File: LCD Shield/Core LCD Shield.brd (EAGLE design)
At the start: 38.1 x 35.6 mm, 9 parts, among them IC1 MC33269T-5.0, J1 TWIG_2.0-DIP-FEMALE

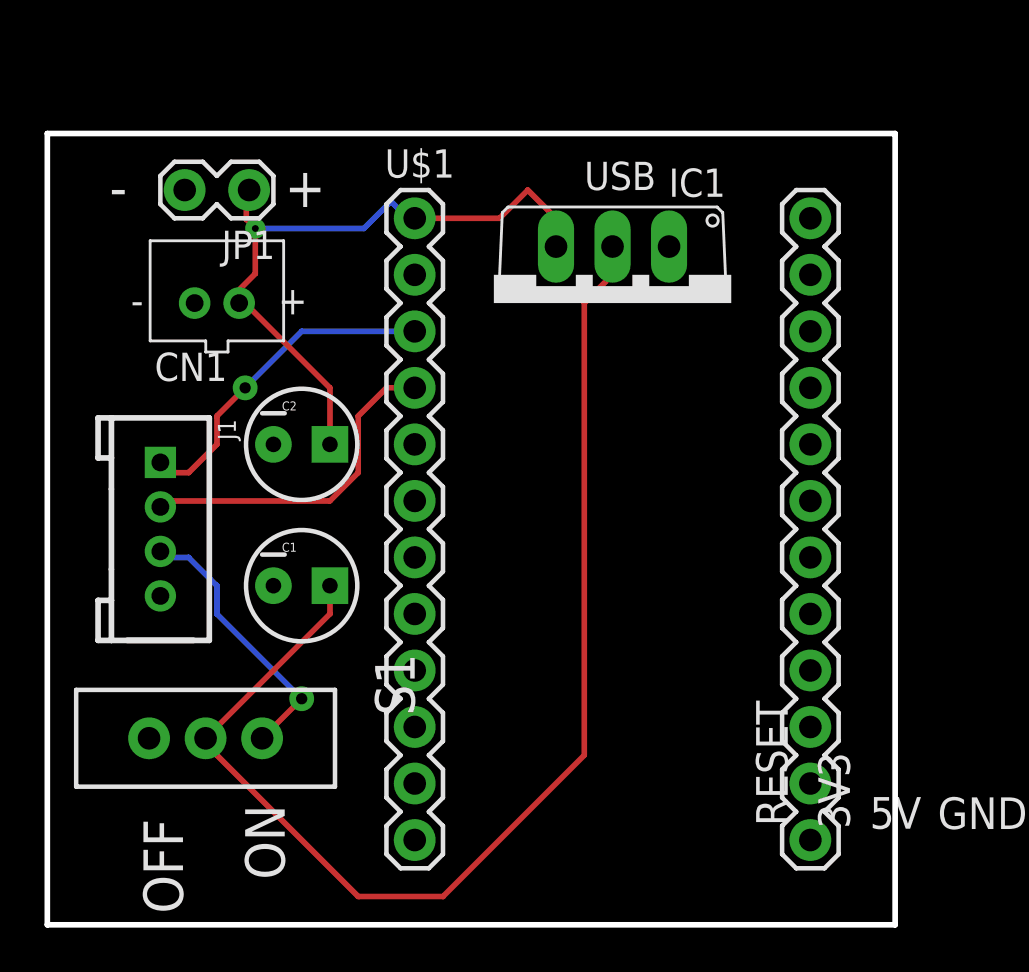
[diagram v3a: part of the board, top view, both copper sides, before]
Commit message: Fixed LCD Shield, upgraded to v0.2
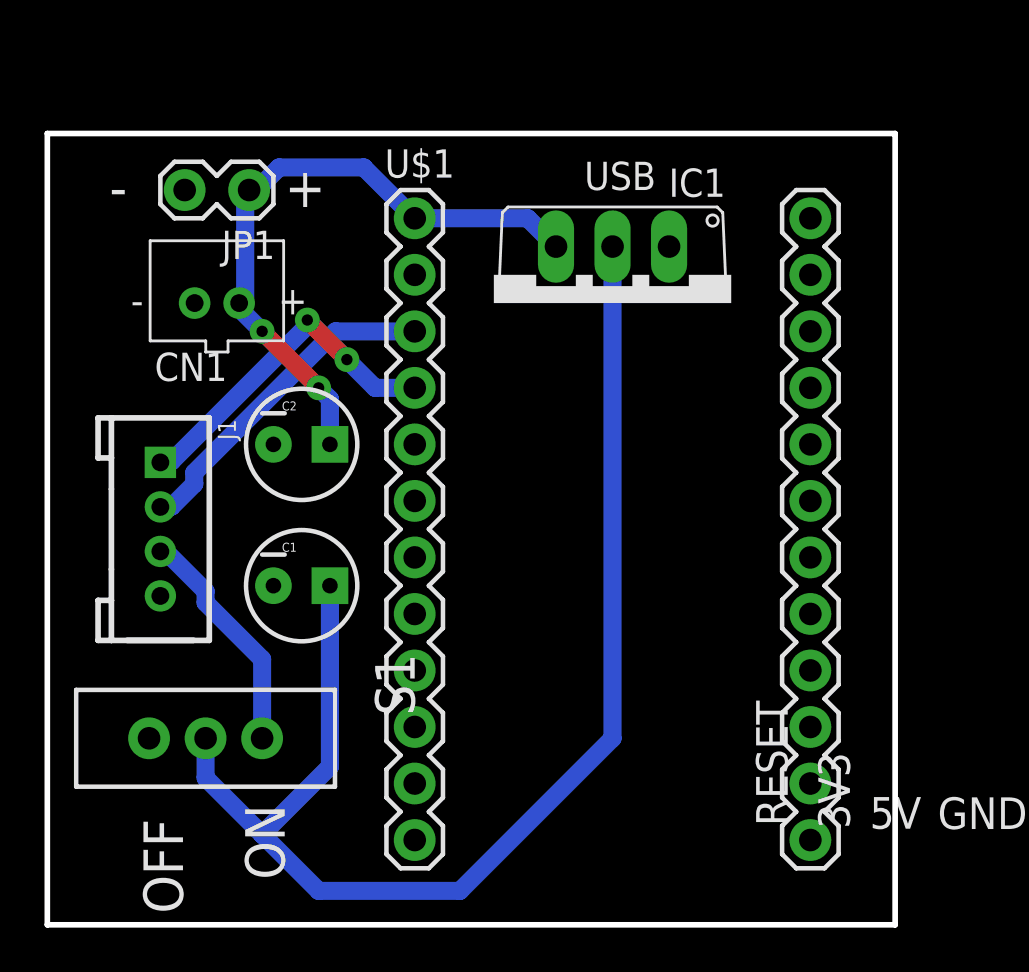
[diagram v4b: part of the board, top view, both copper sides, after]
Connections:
- net RX: now also J1.1; no longer J1.2
- net TX: now also J1.2; no longer J1.1
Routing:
- net N1: track 55.2 -> 59.5 mm
- net +5V: track 12.5 -> 10.8 mm, vias 1 -> 0
- net VIN: track 30.6 -> 29.1 mm, vias 1 -> 2
- net TX: track 15.3 -> 15.0 mm, vias 1 -> 0
- net RX: track 15.3 -> 15.5 mm, vias 0 -> 2
- removed copper zone on layer 16, net GND
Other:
- board text added: "Spark LCD Shield v0.2 2013-04-17"
- board text removed: "Spark LCD Shield v0.1 2013-04-08"
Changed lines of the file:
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@@
 <setting verticaltext="up"/>
 </settings>
-<grid distance="0.05" unitdist="inch" unit="inch" style="lines" multiple="1" display="yes" altdistance="0.005" altunitdist="inch" altunit="inch"/>
+<grid distance="0.01" unitdist="inch" unit="inch" style="lines" multiple="1" display="yes" altdistance="0.005" altunitdist="inch" altunit="inch"/>
 <layers>
 <layer number="1" name="Top" color="4" fill="1" visible="yes" active="yes"/>
@@
 <text x="24.13" y="33.02" size="1.27" layer="21" font="vector" ratio="15">USB</text>
 <text x="22.86" y="2.54" size="1.27" layer="22" font="vector" ratio="15" rot="MR90">Spark LCD Shield
-v0.1
-2013-04-08</text>
+v0.2
+2013-04-17</text>
 </plain>
 <attributes>
@@
 <contactref element="S1" pad="1"/>
 <contactref element="J1" pad="3"/>
-<wire x1="11.43" y1="10.16" x2="9.652" y2="8.382" width="0.254" layer="1"/>
-<wire x1="7.62" y1="13.97" x2="11.43" y2="10.16" width="0.254" layer="16"/>
-<wire x1="7.62" y1="15.24" x2="7.62" y2="13.97" width="0.254" layer="16"/>
-<wire x1="6.35" y1="16.51" x2="7.62" y2="15.24" width="0.254" layer="16"/>
-<wire x1="5.08" y1="16.51" x2="6.35" y2="16.51" width="0.254" layer="16"/>
-<wire x1="5.08" y1="16.51" x2="5.08" y2="16.78" width="0.254" layer="16"/>
-<via x="11.43" y="10.16" extent="1-16" drill="0.508"/>
+<wire x1="9.652" y1="11.938" x2="9.652" y2="8.382" width="0.8128" layer="16"/>
+<wire x1="7.112" y1="14.478" x2="9.652" y2="11.938" width="0.8128" layer="16"/>
+<wire x1="7.112" y1="14.986" x2="7.112" y2="14.478" width="0.8128" layer="16"/>
+<wire x1="5.08" y1="17.018" x2="7.112" y2="14.986" width="0.8128" layer="16"/>
+<wire x1="5.08" y1="17.018" x2="5.08" y2="16.78" width="0.8128" layer="16"/>
 </signal>
 <signal name="GND">
@@
 <contactref element="JP1" pad="2"/>
 <contactref element="J1" pad="4"/>
-<polygon width="0.254" layer="16">
-<vertex x="0" y="0"/>
-<vertex x="0" y="35.56"/>
-<vertex x="38.1" y="35.56"/>
-<vertex x="38.1" y="0"/>
-</polygon>
 <polygon width="0.254" layer="1">
 <vertex x="0" y="0"/>
@@
 <contactref element="CN1" pad="1"/>
 <contactref element="JP1" pad="1"/>
-<wire x1="8.5344" y1="28.448" x2="8.5344" y2="28.0416" width="0.254" layer="1"/>
-<wire x1="9.3472" y1="29.2608" x2="8.5344" y2="28.448" width="0.254" layer="1"/>
-<wire x1="9.3472" y1="31.2928" x2="9.3472" y2="29.2608" width="0.254" layer="1"/>
-<wire x1="8.9408" y1="31.6992" x2="9.3472" y2="31.2928" width="0.254" layer="1"/>
-<wire x1="8.9408" y1="32.9184" x2="8.9408" y2="31.6992" width="0.254" layer="1"/>
-<wire x1="8.5344" y1="28.0416" x2="8.62" y2="27.94" width="0.254" layer="1"/>
-<wire x1="8.9408" y1="32.9184" x2="9.0678" y2="33.02" width="0.254" layer="1"/>
-<wire x1="14.224" y1="31.2928" x2="9.3472" y2="31.2928" width="0.254" layer="16"/>
-<wire x1="15.4432" y1="32.512" x2="14.224" y2="31.2928" width="0.254" layer="16"/>
-<wire x1="16.256" y1="31.6992" x2="15.4432" y2="32.512" width="0.254" layer="16"/>
-<wire x1="16.256" y1="31.6992" x2="16.51" y2="31.75" width="0.254" layer="16"/>
-<via x="9.3472" y="31.2928" extent="1-16" drill="0.3048"/>
-<wire x1="12.7" y1="24.13" x2="12.7" y2="21.59" width="0.254" layer="1"/>
-<wire x1="8.89" y1="27.94" x2="12.7" y2="24.13" width="0.254" layer="1"/>
-<wire x1="8.89" y1="27.94" x2="8.62" y2="27.94" width="0.254" layer="1"/>
-<wire x1="20.32" y1="31.75" x2="16.51" y2="31.75" width="0.254" layer="1"/>
-<wire x1="21.59" y1="33.02" x2="20.32" y2="31.75" width="0.254" layer="1"/>
-<wire x1="22.86" y1="31.75" x2="21.59" y2="33.02" width="0.254" layer="1"/>
-<wire x1="22.86" y1="30.48" x2="22.86" y2="31.75" width="0.254" layer="1"/>
+<wire x1="21.59" y1="31.75" x2="16.51" y2="31.75" width="0.8128" layer="16"/>
+<wire x1="22.86" y1="30.48" x2="21.59" y2="31.75" width="0.8128" layer="16"/>
+<wire x1="8.89" y1="28.194" x2="8.89" y2="33.02" width="0.8128" layer="16"/>
+<wire x1="8.636" y1="27.94" x2="8.89" y2="28.194" width="0.8128" layer="16"/>
+<wire x1="8.89" y1="33.02" x2="9.0678" y2="33.02" width="0.8128" layer="16"/>
+<wire x1="8.636" y1="27.94" x2="8.62" y2="27.94" width="0.8128" layer="16"/>
+<wire x1="10.414" y1="34.036" x2="9.398" y2="33.02" width="0.8128" layer="16"/>
+<wire x1="14.224" y1="34.036" x2="10.414" y2="34.036" width="0.8128" layer="16"/>
+<wire x1="16.51" y1="31.75" x2="14.224" y2="34.036" width="0.8128" layer="16"/>
+<wire x1="9.398" y1="33.02" x2="9.0678" y2="33.02" width="0.8128" layer="16"/>
+<wire x1="12.7" y1="23.622" x2="12.7" y2="21.59" width="0.8128" layer="16"/>
+<wire x1="12.192" y1="24.13" x2="12.7" y2="23.622" width="0.8128" layer="16"/>
+<wire x1="9.652" y1="26.67" x2="12.192" y2="24.13" width="0.8128" layer="1"/>
+<wire x1="8.636" y1="27.686" x2="9.652" y2="26.67" width="0.8128" layer="16"/>
+<wire x1="8.636" y1="27.686" x2="8.62" y2="27.94" width="0.8128" layer="16"/>
+<via x="12.192" y="24.13" extent="1-16" drill="0.508"/>
+<via x="9.652" y="26.67" extent="1-16" drill="0.508"/>
 </signal>
 <signal name="N1">
@@
 <contactref element="C1" pad="1"/>
 <contactref element="S1" pad="2"/>
-<wire x1="12.7" y1="13.97" x2="7.112" y2="8.382" width="0.254" layer="1"/>
-<wire x1="12.7" y1="15.24" x2="12.7" y2="13.97" width="0.254" layer="1"/>
-<wire x1="13.97" y1="1.27" x2="7.62" y2="7.62" width="0.254" layer="1"/>
-<wire x1="17.78" y1="1.27" x2="13.97" y2="1.27" width="0.254" layer="1"/>
-<wire x1="24.13" y1="7.62" x2="17.78" y2="1.27" width="0.254" layer="1"/>
-<wire x1="24.13" y1="27.94" x2="24.13" y2="7.62" width="0.254" layer="1"/>
-<wire x1="25.4" y1="29.21" x2="24.13" y2="27.94" width="0.254" layer="1"/>
-<wire x1="25.4" y1="30.48" x2="25.4" y2="29.21" width="0.254" layer="1"/>
-<wire x1="7.62" y1="7.62" x2="7.112" y2="8.382" width="0.254" layer="1"/>
+<wire x1="25.4" y1="8.382" x2="25.4" y2="30.48" width="0.8128" layer="16"/>
+<wire x1="18.542" y1="1.524" x2="25.4" y2="8.382" width="0.8128" layer="16"/>
+<wire x1="12.192" y1="1.524" x2="18.542" y2="1.524" width="0.8128" layer="16"/>
+<wire x1="7.112" y1="6.604" x2="9.652" y2="4.064" width="0.8128" layer="16"/>
+<wire x1="9.652" y1="4.064" x2="12.192" y2="1.524" width="0.8128" layer="16"/>
+<wire x1="7.112" y1="8.382" x2="7.112" y2="6.604" width="0.8128" layer="16"/>
+<wire x1="12.7" y1="7.112" x2="9.652" y2="4.064" width="0.8128" layer="16"/>
+<wire x1="12.7" y1="15.24" x2="12.7" y2="7.112" width="0.8128" layer="16"/>
 </signal>
 <signal name="VDDA">
@@
 </signal>
 <signal name="RX">
-<contactref element="J1" pad="2"/>
 <contactref element="U$1" pad="4"/>
-<wire x1="5.08" y1="19.05" x2="12.7" y2="19.05" width="0.254" layer="1"/>
-<wire x1="5.08" y1="19.05" x2="5.08" y2="18.78" width="0.254" layer="1"/>
-<wire x1="13.97" y1="20.32" x2="12.7" y2="19.05" width="0.254" layer="1"/>
-<wire x1="13.97" y1="22.86" x2="13.97" y2="20.32" width="0.254" layer="1"/>
-<wire x1="15.24" y1="24.13" x2="13.97" y2="22.86" width="0.254" layer="1"/>
-<wire x1="16.51" y1="24.13" x2="15.24" y2="24.13" width="0.254" layer="1"/>
+<contactref element="J1" pad="1"/>
+<wire x1="5.588" y1="20.828" x2="5.08" y2="20.828" width="0.8128" layer="16"/>
+<wire x1="11.684" y1="26.924" x2="5.588" y2="20.828" width="0.8128" layer="16"/>
+<wire x1="11.684" y1="27.178" x2="11.684" y2="26.924" width="0.8128" layer="16"/>
+<wire x1="13.462" y1="25.4" x2="11.684" y2="27.178" width="0.8128" layer="1"/>
+<wire x1="14.732" y1="24.13" x2="13.462" y2="25.4" width="0.8128" layer="16"/>
+<wire x1="16.51" y1="24.13" x2="14.732" y2="24.13" width="0.8128" layer="16"/>
+<wire x1="5.08" y1="20.828" x2="5.08" y2="20.78" width="0.8128" layer="16"/>
+<via x="11.684" y="27.178" extent="1-16" drill="0.508"/>
+<via x="13.462" y="25.4" extent="1-16" drill="0.508"/>
 </signal>
 <signal name="TX">
-<contactref element="J1" pad="1"/>
 <contactref element="U$1" pad="3"/>
-<wire x1="5.08" y1="20.32" x2="6.35" y2="20.32" width="0.254" layer="1"/>
-<wire x1="5.08" y1="20.32" x2="5.08" y2="20.78" width="0.254" layer="1"/>
-<wire x1="7.62" y1="21.59" x2="6.35" y2="20.32" width="0.254" layer="1"/>
-<wire x1="7.62" y1="22.86" x2="7.62" y2="21.59" width="0.254" layer="1"/>
-<wire x1="8.89" y1="24.13" x2="7.62" y2="22.86" width="0.254" layer="1"/>
-<wire x1="11.43" y1="26.67" x2="8.89" y2="24.13" width="0.254" layer="16"/>
-<wire x1="16.51" y1="26.67" x2="11.43" y2="26.67" width="0.254" layer="16"/>
-<via x="8.89" y="24.13" extent="1-16" drill="0.508"/>
+<contactref element="J1" pad="2"/>
+<wire x1="12.954" y1="26.67" x2="16.51" y2="26.67" width="0.8128" layer="16"/>
+<wire x1="6.604" y1="20.32" x2="12.954" y2="26.67" width="0.8128" layer="16"/>
+<wire x1="6.604" y1="19.812" x2="6.604" y2="20.32" width="0.8128" layer="16"/>
+<wire x1="5.588" y1="18.796" x2="6.604" y2="19.812" width="0.8128" layer="16"/>
+<wire x1="5.08" y1="18.796" x2="5.588" y2="18.796" width="0.8128" layer="16"/>
+<wire x1="5.08" y1="18.796" x2="5.08" y2="18.78" width="0.8128" layer="16"/>
 </signal>
 <signal name="VCC">
